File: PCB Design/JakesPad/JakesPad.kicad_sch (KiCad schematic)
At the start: 30 parts, among them SW1 SW_Push, SW2 SW_Push, SW3 SW_Push, SW4 SW_Push, SW5 SW_Push, SW6 SW_Push, U2 rp2040-zero

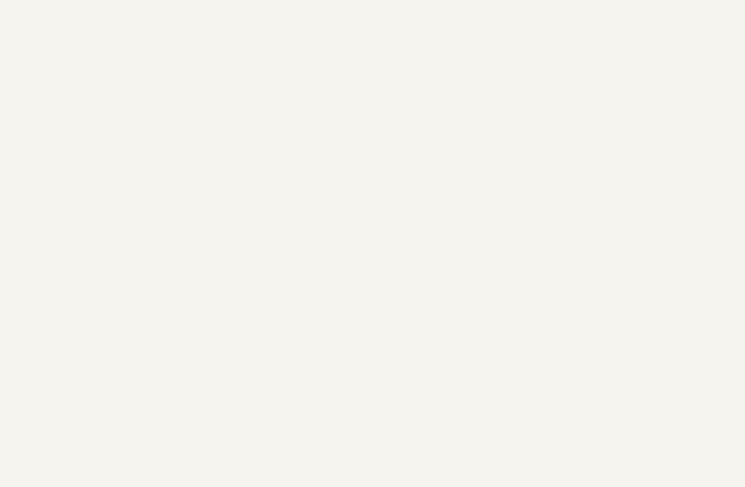
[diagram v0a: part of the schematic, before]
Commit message: Need to update component placement and add RGB.
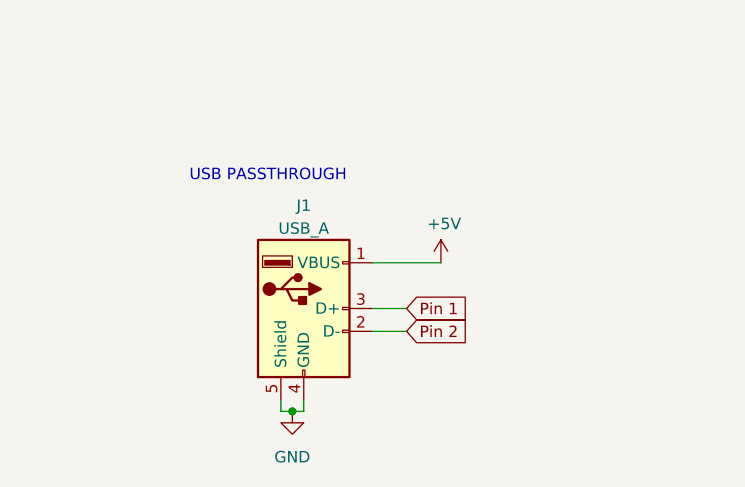
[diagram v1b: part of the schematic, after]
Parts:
- added J1: USB_A, symbol Connector:USB_A
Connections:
- net +5V: now also J1.1 (VBUS)
- net GND: now also J1.4 (GND), J1.5 (Shield)
- new net Pin 1: J1.3 (D+)
- new net Pin 2: J1.2 (D-)
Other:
- note added: "USB PASSTHROUGH"
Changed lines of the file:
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@@
   (junction (at 97.79 53.34) (diameter 0) (color 0 0 0 0)
+  )
+  (junction (at 45.72 185.42) (diameter 0) (color 0 0 0 0)
   )
   (no_connect (at 128.27 50.8))
@@
     (stroke (width 0) (type default))
   )
+  (wire (pts (xy 62.23 168.91) (xy 54.61 168.91))
+    (stroke (width 0) (type default))
+  )
   (wire (pts (xy 143.51 63.5) (xy 143.51 55.88))
     (stroke (width 0) (type default))
@@
     (stroke (width 0) (type default))
   )
+  (wire (pts (xy 54.61 176.53) (xy 58.42 176.53))
+    (stroke (width 0) (type default))
+  )
   (wire (pts (xy 90.17 124.46) (xy 118.11 124.46))
     (stroke (width 0) (type default))
@@
     (stroke (width 0) (type default))
   )
+  (wire (pts (xy 44.45 185.42) (xy 44.45 184.15))
+    (stroke (width 0) (type default))
+  )
   (wire (pts (xy 83.82 92.71) (xy 83.82 100.33))
     (stroke (width 0) (type default))
@@
     (stroke (width 0) (type default))
   )
+  (wire (pts (xy 46.99 185.42) (xy 46.99 184.15))
+    (stroke (width 0) (type default))
+  )
   (wire (pts (xy 189.23 58.42) (xy 189.23 59.69))
     (stroke (width 0) (type default))
@@
     (stroke (width 0) (type default))
   )
+  (wire (pts (xy 45.72 185.42) (xy 46.99 185.42))
+    (stroke (width 0) (type default))
+  )
   (wire (pts (xy 83.82 73.66) (xy 83.82 87.63))
     (stroke (width 0) (type default))
@@
     (stroke (width 0) (type default))
   )
+  (wire (pts (xy 45.72 185.42) (xy 44.45 185.42))
+    (stroke (width 0) (type default))
+  )
   (wire (pts (xy 88.9 57.15) (xy 100.33 57.15))
     (stroke (width 0) (type default))
@@
   (wire (pts (xy 72.39 63.5) (xy 102.87 63.5))
     (stroke (width 0) (type default))
+  )
+  (wire (pts (xy 54.61 173.99) (xy 58.42 173.99))
+    (stroke (width 0) (type default))
+  )
+  (text "USB PASSTHROUGH" (at 34.29 160.02 0)
+    (effects (font (size 1.27 1.27)) (justify left bottom))
   )
   (text "JakesPad FightPad Controller PCB" (at 15.24 22.86 0)
@@
     (effects (font (size 1.27 1.27)) (justify left bottom))
   )
+  (global_label "Pin 1" (shape input) (at 58.42 173.99 0) (fields_autoplaced)
+    (effects (font (size 1.27 1.27)) (justify left))
+    (property "Intersheetrefs" "${INTERSHEET_REFS}" (at 66.6218 173.99 0)
+      (effects (font (size 1.27 1.27)) (justify left) hide)
+    )
+  )
+  (global_label "Pin 2" (shape input) (at 58.42 176.53 0) (fields_autoplaced)
+    (effects (font (size 1.27 1.27)) (justify left))
+    (property "Intersheetrefs" "${INTERSHEET_REFS}" (at 66.6218 176.53 0)
+      (effects (font (size 1.27 1.27)) (justify left) hide)
+    )
+  )
   (symbol (lib_id "Switch:SW_Push") (at 55.88 86.36 0) (unit 1)
     (in_bom yes) (on_board yes) (dnp no) (fields_autoplaced)
@@
         (path "/e63e39d7-6ac0-4ffd-8aa3-1841a4541b55"
           (reference "A2") (unit 1)
+        )
+      )
+    )
+  )
+  (symbol (lib_id "power:GND") (at 45.72 185.42 0) (unit 1)
+    (in_bom yes) (on_board yes) (dnp no) (fields_autoplaced)
+    (property "Reference" "#PWR028" (at 45.72 191.77 0)
+      (effects (font (size 1.27 1.27)) hide)
+    )
+    (property "Value" "GND" (at 45.72 190.5 0)
+      (effects (font (size 1.27 1.27)))
+    )
+    (property "Footprint" "" (at 45.72 185.42 0)
+      (effects (font (size 1.27 1.27)) hide)
+    )
+    (property "Datasheet" "" (at 45.72 185.42 0)
+      (effects (font (size 1.27 1.27)) hide)
+    )
+    (pin "1")
+    (instances
+      (project "JakesPad"
+        (path "/e63e39d7-6ac0-4ffd-8aa3-1841a4541b55"
+          (reference "#PWR028") (unit 1)
         )
       )
@@
         (path "/e63e39d7-6ac0-4ffd-8aa3-1841a4541b55"
           (reference "#PWR025") (unit 1)
+        )
+      )
+    )
+  )
+  (symbol (lib_id "power:+5V") (at 62.23 168.91 0) (unit 1)
+    (in_bom yes) (on_board yes) (dnp no)
+    (property "Reference" "#PWR027" (at 62.23 172.72 0)
+      (effects (font (size 1.27 1.27)) hide)
+    )
+    (property "Value" "+5V" (at 62.5983 164.5856 0)
+      (effects (font (size 1.27 1.27)))
+    )
+    (property "Footprint" "" (at 62.23 168.91 0)
+      (effects (font (size 1.27 1.27)))
+    )
+    (property "Datasheet" "" (at 62.23 168.91 0)
+      (effects (font (size 1.27 1.27)))
+    )
+    (pin "1")
+    (instances
+      (project "JakesPad"
+        (path "/e63e39d7-6ac0-4ffd-8aa3-1841a4541b55"
+          (reference "#PWR027") (unit 1)
         )
       )
@@
         )
       )
+    )
+  )
+  (symbol (lib_id "Connector:USB_A") (at 46.99 173.99 0) (unit 1)
+    (in_bom yes) (on_board yes) (dnp no) (fields_autoplaced)
+    (property "Reference" "J1" (at 46.99 162.56 0)
+      (effects (font (size 1.27 1.27)))
+    )
+    (property "Value" "USB_A" (at 46.99 165.1 0)
+      (effects (font (size 1.27 1.27)))
+    )
+    (property "Footprint" "" (at 50.8 175.26 0)
+      (effects (font (size 1.27 1.27)) hide)
+    )
+    (property "Datasheet" " ~" (at 50.8 175.26 0)
+      (effects (font (size 1.27 1.27)) hide)
+    )
+    (pin "1")
+    (pin "2")
+    (pin "3")
+    (pin "4")
+    (pin "5")
+    (instances
+      (project "JakesPad"
+        (path "/e63e39d7-6ac0-4ffd-8aa3-1841a4541b55"
+          (reference "J1") (unit 1)
+        )
+      )
